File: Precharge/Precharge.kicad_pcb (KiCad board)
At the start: 2 copper layers, 133 x 98 mm, 121 parts, among them J1 MicroFit, J2 Mini-Fit_Jr_5566-04A, J3 Micro-Fit 43045-0212, K1 OMRON-G2RL-24, K2 G7L-2A-X-L, Q1 2N7002, Q2 MMBT3906, Q3 2N7002, U1 TJA1051T-3, U10 LM393, U11 4N35, U2 SPAN02A-12, U3 Teensy4.0, U4 LM1117-5.0, U5 4N35, U6 4N35, U7 LM331, U8 LM331, U9 LM2904

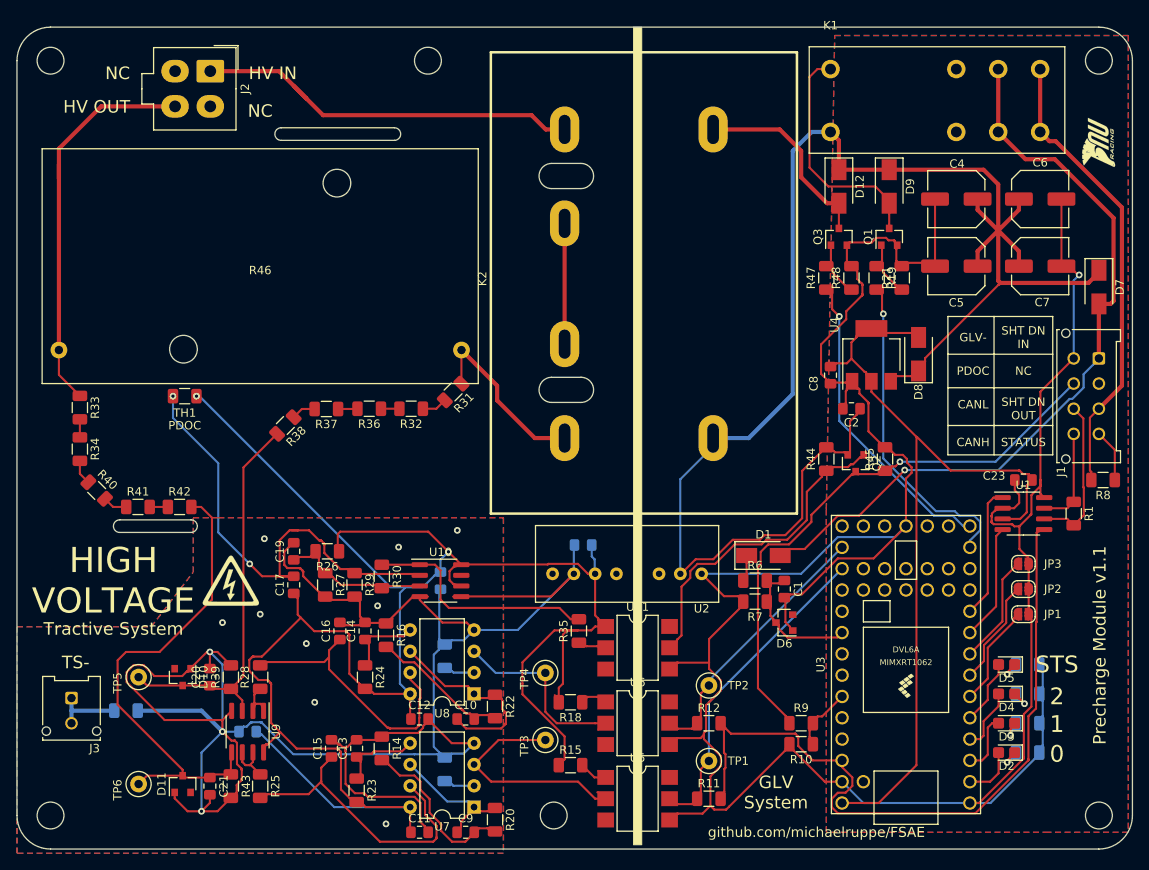
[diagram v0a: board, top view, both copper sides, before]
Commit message: RML through hole part 1
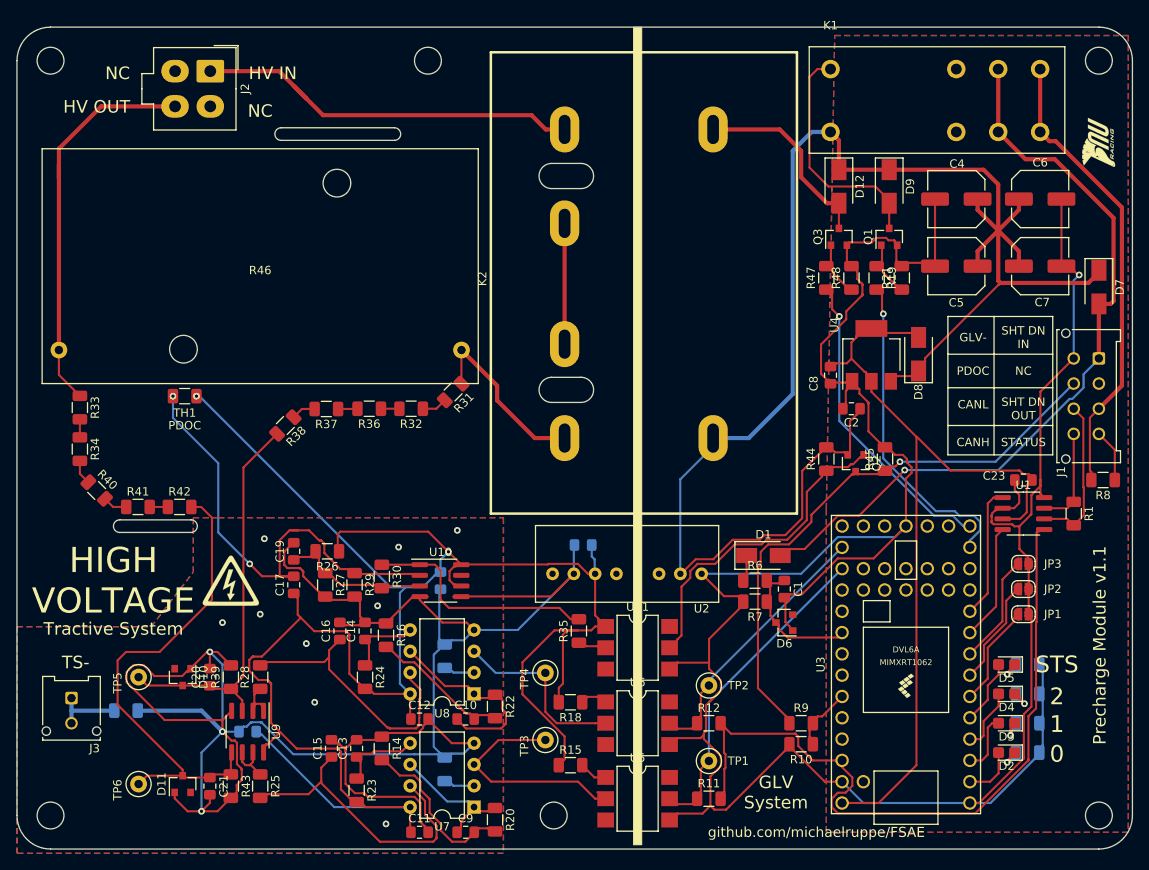
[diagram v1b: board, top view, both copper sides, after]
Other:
- net class Default removed
